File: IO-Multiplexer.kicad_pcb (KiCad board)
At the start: 2 copper layers, 53.3 x 127 mm, 18 parts

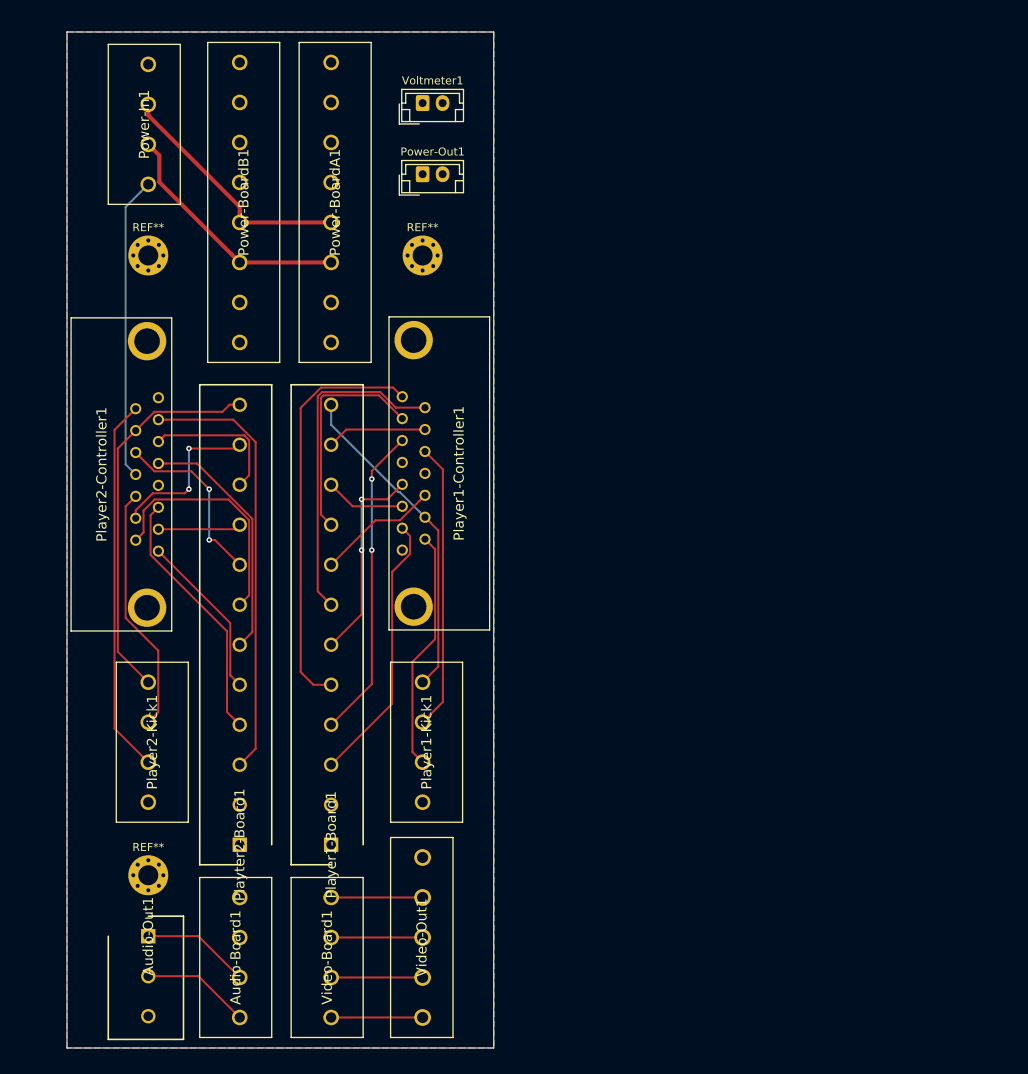
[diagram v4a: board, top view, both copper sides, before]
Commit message: Update to neo-geo plus pinout
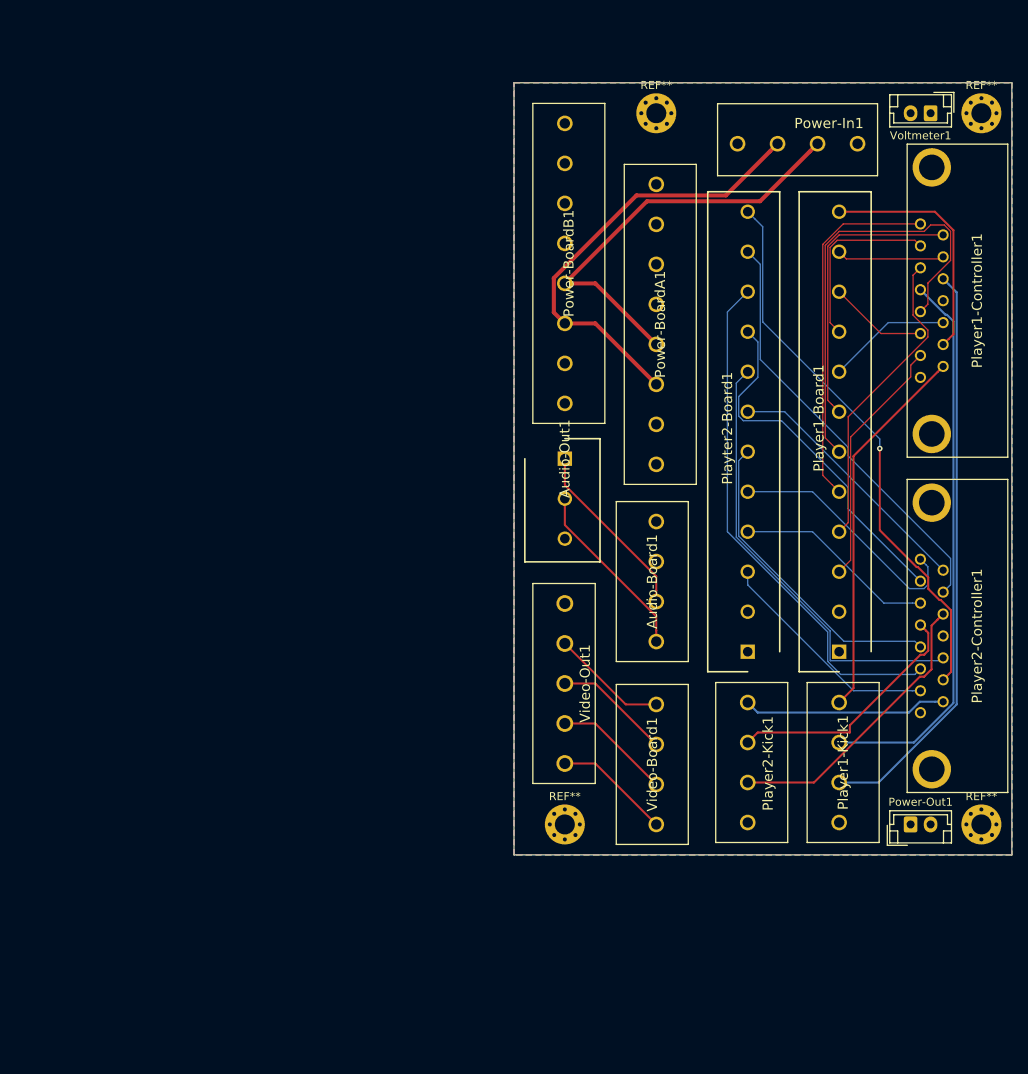
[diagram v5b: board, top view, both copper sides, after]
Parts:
- removed the REF** at (154.9, 120.7)
- added REF**: MountingHole_2.5mm_Pad_Via, MountingHole:MountingHole_2.5mm_Pad_Via, F.Cu at (259.1, 114.3)
- added REF**: MountingHole_2.5mm_Pad_Via, MountingHole:MountingHole_2.5mm_Pad_Via, F.Cu at (218.4, 25.4)
- moved REF** 105.6 mm to (259.1, 25.4)
- moved Player2-Controller1 103.1 mm to (251.5, 100.3), turned to 90 degrees
- moved Power-Out1 101.6 mm to (250.2, 114.3)
- moved Audio-Out1 79.2 mm to (207.0, 68.6)
- moved Player2-Kick1 75.0 mm to (229.9, 99.1)
- moved Power-In1 73.8 mm to (228.6, 29.2), turned to 0 degrees
- moved REF** 73.3 mm to (207.0, 114.3)
- moved Audio-Board1 70.1 mm to (218.4, 91.4)
- moved Player1-Controller1 68.3 mm to (251.5, 58.4)
- moved Player1-Board1 67.9 mm to (241.3, 92.7)
- moved Playter2-Board1 67.9 mm to (229.9, 92.7)
- moved Voltmeter1 63.5 mm to (252.7, 25.4), turned to 180 degrees
- moved Player1-Kick1 52.1 mm to (241.3, 99.1)
- moved Video-Board1 47.3 mm to (218.4, 114.3)
- moved Power-BoardA1 43.4 mm to (218.4, 34.3)
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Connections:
- Player1-Controller1 pad 10: /P1-Button5 -> /P1-Button7
- Player1-Controller1 pad 2: /P1-Button6 -> /P1-Button5
- Player1-Controller1 pad 9: Net-(Player1-Controller1-Pad9) -> /P1-Button6
- Player1-Kick1 pad 1: /P1-Button4 -> /P1-Button5
- Player1-Kick1 pad 2: /P1-Button5 -> /P1-Button6
- Player1-Kick1 pad 3: /P1-Button6 -> /P1-Button7
- Player2-Controller1 pad 10: /P2-Button5 -> /P2-Button7
- Player2-Controller1 pad 2: /P2-Button6 -> /P2-Button5
- Player2-Controller1 pad 9: Net-(Player2-Controller1-Pad9) -> /P2-Button6
- Player2-Kick1 pad 1: /P2-Button4 -> /P2-Button5
- Player2-Kick1 pad 2: /P2-Button5 -> /P2-Button6
- Player2-Kick1 pad 3: /P2-Button6 -> /P2-Button7
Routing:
- net /P1-Button7: track 0.00 -> 72.6 mm
- net /P2-Button2: track 18.0 -> 65.0 mm
- net /P1-Button6: track 30.1 -> 69.8 mm
- net /+5V: track 38.0 -> 0.00 mm
- net /P2-Button7: track 0.00 -> 36.4 mm
- net /P2-Button1: track 10.4 -> 44.9 mm
- net /P2-Right: track 22.5 -> 55.8 mm, vias 2 -> 0
- net /P2-Button3: track 20.4 -> 53.4 mm, vias 2 -> 0
- net /P1-Down: track 25.6 -> 55.2 mm, vias 2 -> 0
- net /P2-Coin: track 54.5 -> 28.7 mm
- net /+12V: track 30.9 -> 55.8 mm
- net /-5V: track 30.9 -> 53.4 mm
- net /P2-Button4: track 48.3 -> 69.6 mm, vias 0 -> 1
- net /P2-Button6: track 47.0 -> 31.5 mm
- net /P1-Button5: track 35.8 -> 47.4 mm
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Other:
- board size 53.3 x 127 mm -> 62.2 x 96.5 mm

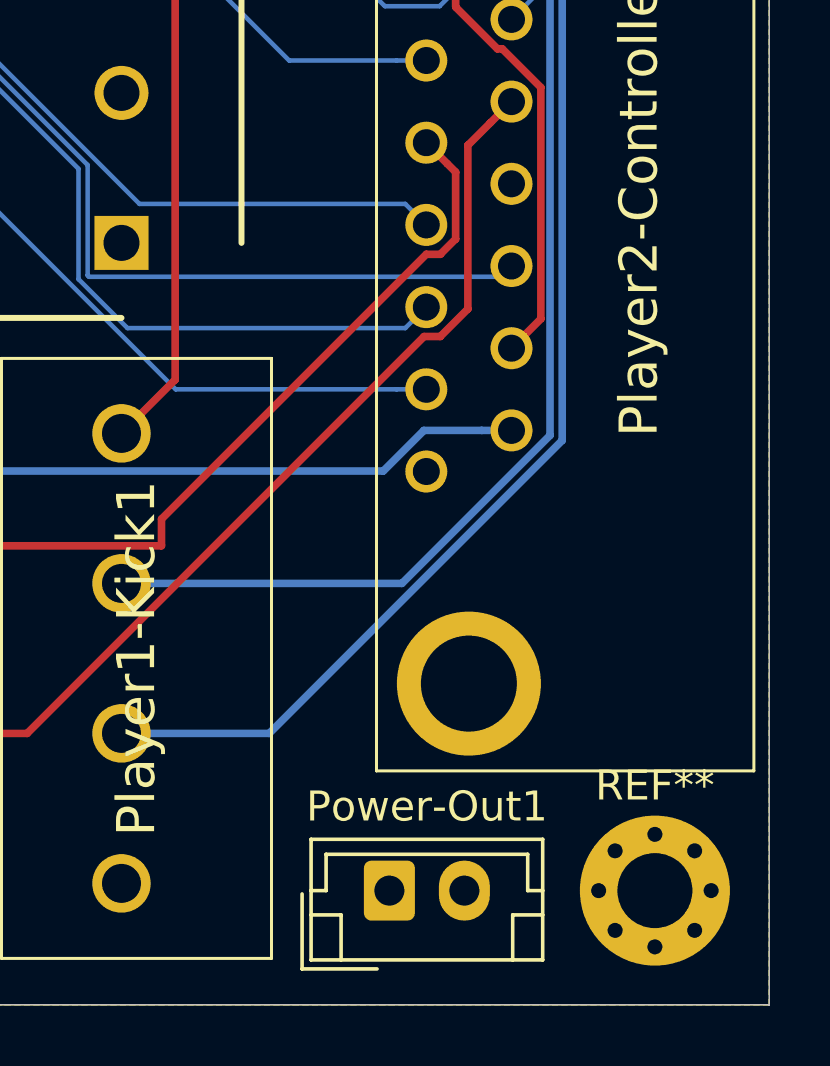
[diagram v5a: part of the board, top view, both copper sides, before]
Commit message: Connecting 5V to P2 since the zone wont fill there
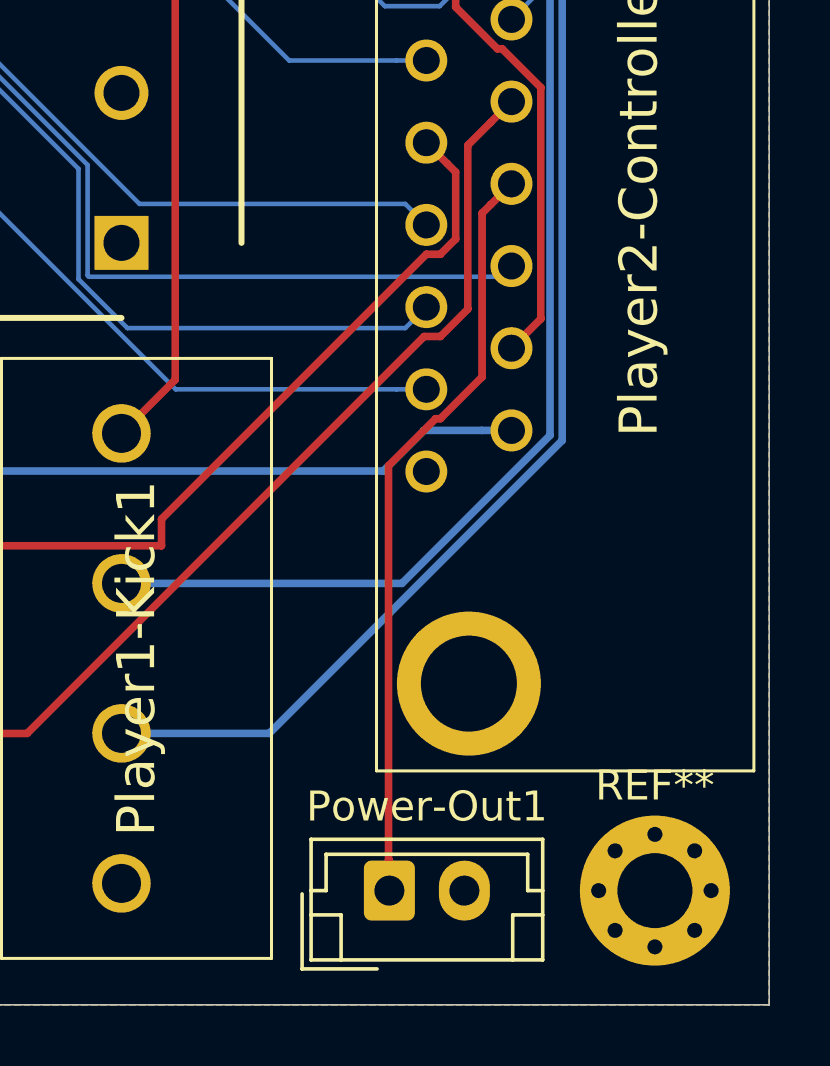
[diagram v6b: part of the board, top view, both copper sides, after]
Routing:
- net /+5V: track 0.00 -> 25.4 mm
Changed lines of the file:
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@@
     (thickness 1.6)
     (drawings 5)
-    (tracks 189)
+    (tracks 198)
     (zones 0)
     (modules 19)
@@
   )
   (setup
-    (last_trace_width 0.1524)
+    (last_trace_width 0.254)
     (user_trace_width 0.254)
     (user_trace_width 0.508)
@@
   (segment (start 218.44 85.061142) (end 218.44 86.44) (width 0.254) (layer F.Cu) (net 8))
   (segment (start 207.01 68.58) (end 207.01 71.866514) (width 0.254) (layer F.Cu) (net 8))
+  (segment (start 253.320599 97.178915) (end 253.320599 91.719401) (width 0.254) (layer F.Cu) (net 9))
+  (segment (start 253.600001 91.439999) (end 254.3 90.74) (width 0.254) (layer F.Cu) (net 9))
+  (segment (start 251.771085 98.569401) (end 251.930113 98.569401) (width 0.254) (layer F.Cu) (net 9))
+  (segment (start 250.200599 100.139887) (end 251.771085 98.569401) (width 0.254) (layer F.Cu) (net 9))
+  (segment (start 250.200599 113.270599) (end 250.200599 100.139887) (width 0.254) (layer F.Cu) (net 9))
+  (segment (start 251.930113 98.569401) (end 253.320599 97.178915) (width 0.254) (layer F.Cu) (net 9))
+  (segment (start 250.23 113.3) (end 250.200599 113.270599) (width 0.254) (layer F.Cu) (net 9))
+  (segment (start 253.320599 91.719401) (end 253.600001 91.439999) (width 0.254) (layer F.Cu) (net 9))
+  (segment (start 250.23 114.3) (end 250.23 113.3) (width 0.254) (layer F.Cu) (net 9))
   (segment (start 210.82 46.67) (end 218.44 54.29) (width 0.508) (layer F.Cu) (net 10))
   (segment (start 207.01 46.67) (end 210.82 46.67) (width 0.508) (layer F.Cu) (net 10))
